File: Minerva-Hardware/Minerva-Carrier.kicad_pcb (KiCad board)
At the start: 4 copper layers, 83.5 x 90 mm, 59 parts, among them J1 HDMI_D_1.4, J11 USB_C_Receptacle_USB2.0, J14 JST_SHBM04B-SRSS-TB, J16 Conn_01x22_Female, J2 Conn_02x07_Odd_Even, J4 Bus_M.2_Socket_M, J5 Conn_01x22_Female, J6 THD-02-R, J8 THD-20-R, Q2 RQ6E080AJ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

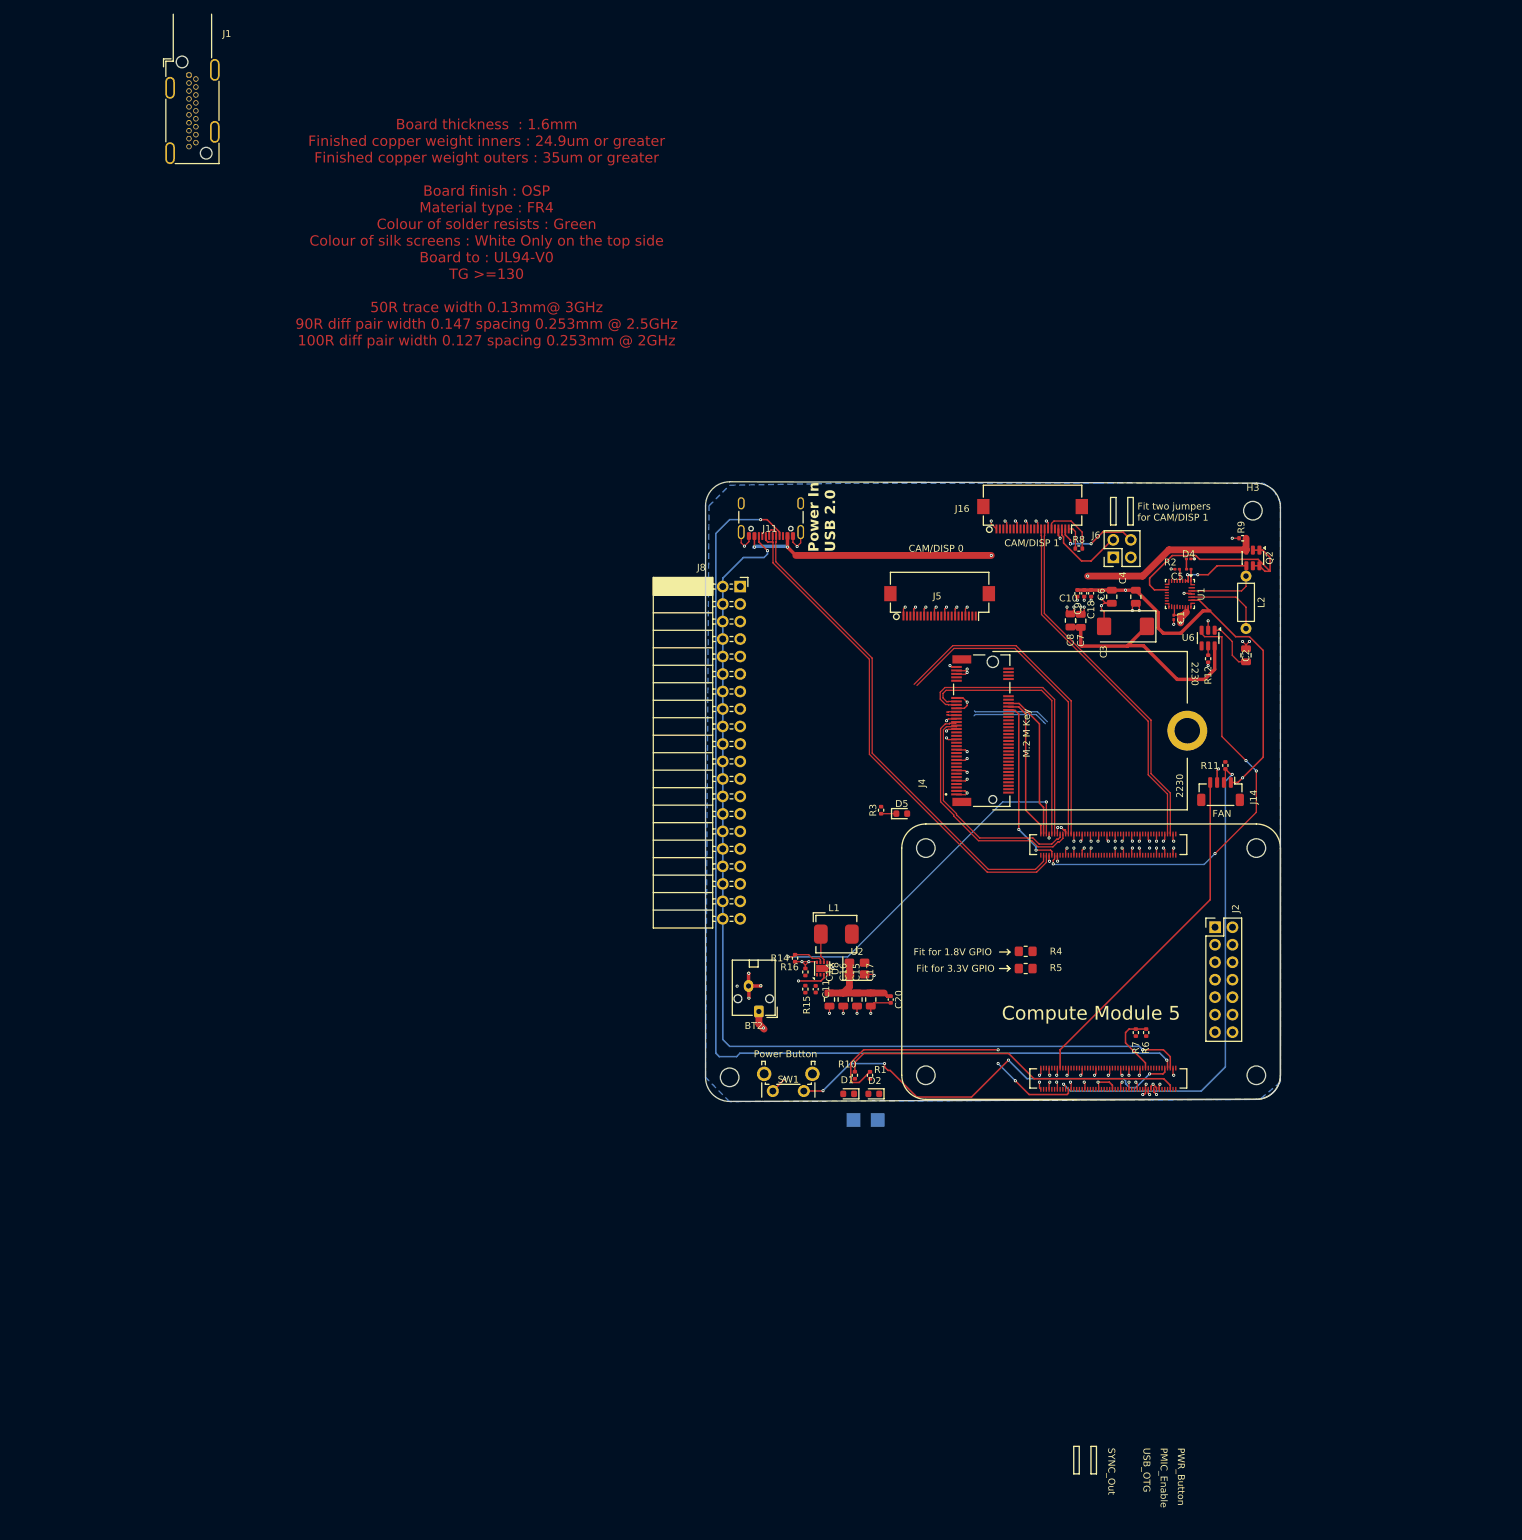
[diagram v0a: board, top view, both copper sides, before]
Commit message: Redid the BQ powerpath unit
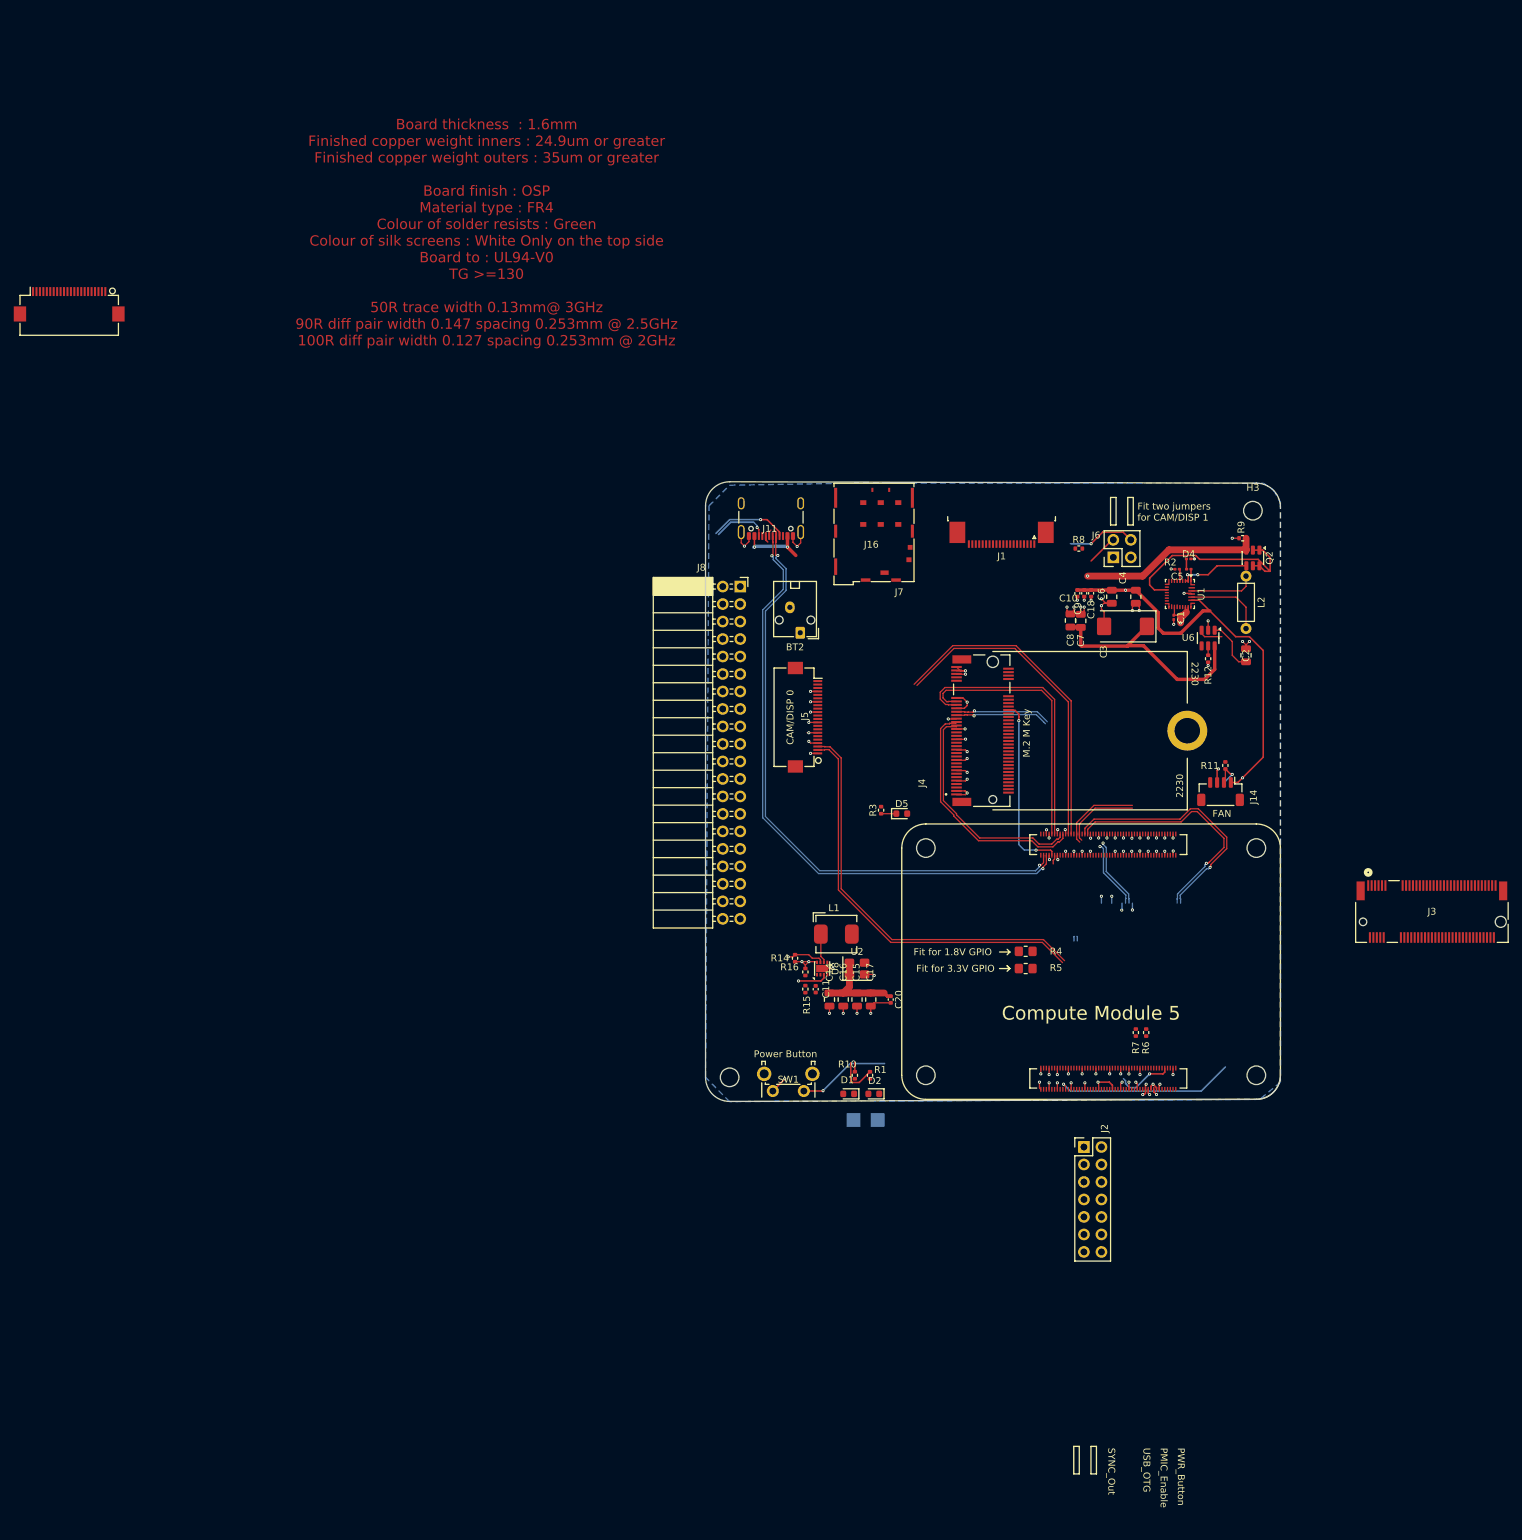
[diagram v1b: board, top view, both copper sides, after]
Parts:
- added J3: Bus_M.2_Socket_B, M.2B:CONN67_2199230_TEC, F.Cu at (193.8, 136.2)
- added J7: JAE_SIM_Card_SF72S006, Connector_JAE:JAE_SIM_Card_SF72S006, F.Cu at (104.4, 75.5)
- J1: footprint Connector_Video:HDMI_A_Kycon_KDMIX-SL1-NS-WS-B15_VerticalRightAngle -> Connector_FFC-FPC:TE_2-1734839-0_1x20-1MP_P0.5mm_Horizontal
- moved J16 143.3 mm to (-13.4, 44.2), turned to 0 degrees
- moved J1 135.6 mm to (122.0, 77.7), turned to 180 degrees
- moved BT2 55.3 mm to (92.8, 91.9)
- moved J2 37.2 mm to (134.0, 166.6)
- moved J5 25.6 mm to (93.5, 104.2), turned to -90 degrees
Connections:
- J1 pad 11: unconnected-(J1-D0--Pad11) -> /CM5_HighSpeed/HDMI_D0_N
- J1 pad 12: unconnected-(J1-CK+-Pad12) -> /CM5_HighSpeed/HDMI_CLK_P
- J1 pad 14: unconnected-(J1-CK--Pad14) -> /CM5_HighSpeed/HDMI_CLK_N
- J1 pad 15: unconnected-(J1-CEC-Pad15) -> /CM5_HighSpeed/HDMI_0_CEC
- J1 pad 16: unconnected-(J1-GND-Pad16) -> GND
- J1 pad 17: unconnected-(J1-SCL-Pad17) -> /CM5_HighSpeed/HDMI0_SCL
- J1 pad 18: unconnected-(J1-SDA-Pad18) -> /CM5_HighSpeed/HDMI0_SDA
- J1 pad 19: unconnected-(J1-+5V-Pad19) -> /CM5_HighSpeed/+5v
- J1 pad 3: unconnected-(J1-D2+-Pad3) -> /CM5_HighSpeed/HDMI_D2_P
- J1 pad 5: unconnected-(J1-D2--Pad5) -> /CM5_HighSpeed/HDMI_D2_N
- J1 pad 6: unconnected-(J1-D1+-Pad6) -> /CM5_HighSpeed/HDMI_D1_P
- J1 pad 8: unconnected-(J1-D1--Pad8) -> /CM5_HighSpeed/HDMI_D1_N
- J1 pad 9: unconnected-(J1-D0+-Pad9) -> /CM5_HighSpeed/HDMI_D0_P
- Module1 pad 151: unconnected-(Module1B-HDMI0_CEC-Pad151) -> /CM5_HighSpeed/HDMI_0_CEC
- Module1 pad 153: unconnected-(Module1B-HDMI0_HOTPLUG-Pad153) -> /CM5_HighSpeed/HDMI_0_HOTPLUG
- Module1 pad 170: unconnected-(Module1B-HDMI0_TX2_P-Pad170) -> /CM5_HighSpeed/HDMI_D2_P
- Module1 pad 172: unconnected-(Module1B-HDMI0_TX2_N-Pad172) -> /CM5_HighSpeed/HDMI_D2_N
- Module1 pad 176: unconnected-(Module1B-HDMI0_TX1_P-Pad176) -> /CM5_HighSpeed/HDMI_D1_P
- Module1 pad 178: unconnected-(Module1B-HDMI0_TX1_N-Pad178) -> /CM5_HighSpeed/HDMI_D1_N
- Module1 pad 182: unconnected-(Module1B-HDMI0_TX0_P-Pad182) -> /CM5_HighSpeed/HDMI_D0_P
- Module1 pad 184: unconnected-(Module1B-HDMI0_TX0_N-Pad184) -> /CM5_HighSpeed/HDMI_D0_N
- Module1 pad 188: unconnected-(Module1B-HDMI0_CLK_P-Pad188) -> /CM5_HighSpeed/HDMI_CLK_P
- Module1 pad 190: unconnected-(Module1B-HDMI0_CLK_N-Pad190) -> /CM5_HighSpeed/HDMI_CLK_N
- Module1 pad 199: unconnected-(Module1B-HDMI0_SDA-Pad199) -> /CM5_HighSpeed/HDMI0_SDA
- Module1 pad 200: unconnected-(Module1B-HDMI0_SCL-Pad200) -> /CM5_HighSpeed/HDMI0_SCL
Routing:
- net /CC1: track 154.4 -> 11.4 mm, vias 2 -> 1
- net /CC2: track 145.8 -> 8.11 mm, vias 3 -> 1
- net /CM5_HighSpeed/VBUS_EN: track 64.7 -> 4.48 mm, vias 4 -> 0
- net /CM5_HighSpeed/DPHY0_D0_P: track 0.00 -> 59.9 mm
- net /CM5_HighSpeed/DPHY0_D0_N: track 0.00 -> 59.5 mm
- net /CM5_HighSpeed/DPHY1_D3_P: track 51.9 -> 0.00 mm
- net /CM5_HighSpeed/DPHY1_D3_N: track 51.9 -> 0.00 mm
- net /CM5_HighSpeed/PCIE_PWR_EN: track 57.0 -> 6.13 mm
- net /CM5_GPIO/TACHO: track 50.5 -> 0.00 mm
- net /CM5_GPIO/nPWR_LED: track 50.2 -> 1.38 mm
- net /CM5_GPIO/PWM: track 71.8 -> 30.3 mm
- net /CM5_GPIO/PWR_BUT: track 62.1 -> 21.8 mm, vias 4 -> 2
- net /CM5_HighSpeed/USB3-0-D_P: track 0.00 -> 36.9 mm, vias 0 -> 1
- net /CM5_HighSpeed/USB3-0-D_N: track 0.00 -> 35.5 mm, vias 0 -> 1
- net Net-(Module1A-LED_nACT): track 43.1 -> 8.18 mm, vias 3 -> 0
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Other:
- board text removed: "CAM/DISP 1"
- board text removed: "Power In USB 2.0"

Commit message: working on pcb more
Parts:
- removed Q2: RQ6E080AJ, Package_TO_SOT_SMD:TSOT-23-6
- added C19: 0.1uF, Capacitor_SMD:C_01005_0402Metric, F.Cu at (252.8, 91.0)
- added C21: 10uF, Capacitor_SMD:C_01005_0402Metric, F.Cu at (252.8, 92.7)
- added C22: 10uF, Capacitor_SMD:C_01005_0402Metric, F.Cu at (252.8, 94.3)
- added C23: 10 uF, Capacitor_SMD:C_0201_0603Metric, F.Cu at (252.9, 99.3)
- added C24: 10uF, Capacitor_SMD:C_01005_0402Metric, F.Cu at (252.8, 96.0)
- added C25: 10uF, Capacitor_SMD:C_01005_0402Metric, F.Cu at (252.8, 97.6)
- added C26: 10uF, Capacitor_SMD:C_01005_0402Metric, F.Cu at (255.0, 91.0)
- added C27: 0.1uF, Capacitor_SMD:C_01005_0402Metric, F.Cu at (255.0, 92.7)
- added C28: 10uF, Capacitor_SMD:C_01005_0402Metric, F.Cu at (255.0, 94.3)
- added C29: 10uF, Capacitor_SMD:C_01005_0402Metric, F.Cu at (255.0, 96.0)
- added C30: 10uF, Capacitor_SMD:C_01005_0402Metric, F.Cu at (255.0, 97.6)
- added C31: 10uF, Capacitor_SMD:C_01005_0402Metric, F.Cu at (257.3, 91.0)
- added C32: 10uF, Capacitor_SMD:C_01005_0402Metric, F.Cu at (257.3, 92.7)
- added C33: 47nF, 25V X7R, Capacitor_SMD:C_01005_0402Metric, F.Cu at (257.3, 94.3)
- added C34: 47nF, 25V X7R, Capacitor_SMD:C_01005_0402Metric, F.Cu at (257.3, 96.0)
- C1: value C_Small_US -> 10 uF
- J3: moved to B.Cu
- L2: value 50 nH -> 1uH; footprint Inductor_THT:L_Axial_L5.3mm_D2.2mm_P7.62mm_Horizontal_Vishay_IM-1 -> CM5 IO Board-rev2:L_Bourns_SRP5030CC
- moved J3 62.8 mm to (131.0, 138.8), turned to 180 degrees
- moved J2 59.6 mm to (192.7, 176.6)
- moved J16 20.1 mm to (3.00, 55.8)
- moved J1 1.76 mm to (120.5, 78.6)
- moved J8 1.57 mm to (85.5, 85.7)
- moved J7 1.20 mm to (104.0, 76.6)
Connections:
- net /CHARGE_IND_SIG renamed +3.3V
- net Net-(U1-SW1) renamed /SW1
- net Net-(U1-SW2) renamed /SW2
- BT2 pad 1: Net-(BT2-+) -> /BATP
- C1 pad 1: Net-(BT2-+) -> /BATP
- C5 pad 1: Net-(U1-REGN) -> /REGN
- D1 pad 2: /+3.3v -> /CM5_GPIO/+3.3v
- D2 pad 2: /+3.3v -> /CM5_GPIO/+3.3v
- J1 pad 1: unconnected-(J1-HPD/HEAC--Pad1) -> /CM5_HighSpeed/HDMI_0_HOTPLUG
- J1 pad 10: unconnected-(J1-D0S-Pad10) -> GND
- J1 pad 13: unconnected-(J1-CKS-Pad13) -> GND
- J1 pad 2: unconnected-(J1-UTILITY/HEAC+-Pad2) -> /CM5_HighSpeed/HDMI_0_HOTPLUG
- J1 pad 4: unconnected-(J1-D2S-Pad4) -> GND
- J1 pad 7: unconnected-(J1-D1S-Pad7) -> GND
- J2 pad 10: /CM5_GPIO/USBOTG -> unconnected-(J2-Pin_10-Pad10)
- J8 pad 1: /+3.3v -> /CM5_GPIO/+3.3v
- J8 pad 17: /+3.3v -> /CM5_GPIO/+3.3v
- Module1 pad 157: /CM5_HighSpeed/USB3-1-RX_N -> GND
- Module1 pad 159: /CM5_HighSpeed/USB3-1-RX_P -> GND
- Module1 pad 163: /CM5_HighSpeed/USB3-1-D_P -> GND
- Module1 pad 165: /CM5_HighSpeed/USB3-1-D_N -> GND
- Module1 pad 169: /CM5_HighSpeed/USB3-1-TX_N -> GND
- Module1 pad 171: /CM5_HighSpeed/USB3-1-TX_P -> GND
- Module1 pad 84: /+3.3v -> /CM5_GPIO/+3.3v
- Module1 pad 86: /+3.3v -> /CM5_GPIO/+3.3v
- R11 pad 1: /+3.3v -> /CM5_GPIO/+3.3v
- R5 pad 1: /+3.3v -> /CM5_GPIO/+3.3v
- U1 pad 10: unconnected-(U1-ACDRV2-Pad10) -> GND
- U1 pad 11: Net-(U1-ACDRV1) -> GND
- U1 pad 12: unconnected-(U1-~{QON}-Pad12) -> /QON
- U1 pad 13: unconnected-(U1-~{CE}-Pad13) -> GND
- U1 pad 16: unconnected-(U1-TS-Pad16) -> Net-(U1-TS)
- U1 pad 17: unconnected-(U1-ILIM_HIZ-Pad17) -> /REGN
- U1 pad 18: Net-(BT2-+) -> Net-(U1-BATP)
- U1 pad 19: unconnected-(U1-BTST2-Pad19) -> /BTST2
- U1 pad 2: Net-(Q2-S) -> /VBUS
- U1 pad 20: unconnected-(U1-PROG-Pad20) -> Net-(U1-PROG)
- U1 pad 22: Net-(BT2-+) -> /BATP
- U1 pad 23: Net-(BT2-+) -> /BATP
- U1 pad 25: /+5v -> /SYS_OUT
- U1 pad 29: unconnected-(U1-PMID-Pad29) -> Net-(U1-PMID)
- U1 pad 3: Net-(Q2-S) -> /VBUS
- U1 pad 4: unconnected-(U1-BTST1-Pad4) -> /BTST1
- U1 pad 5: Net-(U1-REGN) -> /REGN
- U1 pad 8: unconnected-(U1-VAC2-Pad8) -> /VBUS
- U1 pad 9: unconnected-(U1-VAC1-Pad9) -> /VBUS
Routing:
- net (no net): track 0.00 -> 134.8 mm, vias 0 -> 1
- net Net-(BT2-+): track 93.0 -> 0.00 mm, vias 1 -> 0
- net Net-(U1-ACDRV1): track 31.4 -> 0.00 mm
- net Net-(Q2-S): track 10.4 -> 0.00 mm, vias 2 -> 0
- net Net-(U1-SW1): track 0.00 -> 9.67 mm
- net /SW1: track 9.67 -> 0.00 mm
- net Net-(U1-REGN): track 1.62 -> 0.00 mm
- net /REGN: track 0.00 -> 1.62 mm
- net /VBUS: vias 3 -> 5

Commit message: wip shit
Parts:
- moved C7 6.06 mm to (130.0, 85.2)
- moved C8 6.06 mm to (128.5, 85.2)
- turned J1 to 0 degrees
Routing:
- net /CM5_HighSpeed/HDMI_D2_P: track 0.00 -> 54.1 mm
- net /CM5_HighSpeed/HDMI_D2_N: track 0.00 -> 54.1 mm
- net /CM5_HighSpeed/HDMI_D1_P: track 0.00 -> 53.9 mm
- net /CM5_HighSpeed/HDMI_D1_N: track 0.00 -> 53.9 mm
- net /CM5_HighSpeed/HDMI_D0_N: track 0.00 -> 53.8 mm
- net /CM5_HighSpeed/HDMI_D0_P: track 0.00 -> 53.8 mm
- net /CM5_HighSpeed/HDMI_CLK_P: track 0.00 -> 53.7 mm
- net /CM5_HighSpeed/HDMI_CLK_N: track 0.00 -> 53.7 mm
- net /CM5_HighSpeed/DPHY0_D0_P: track 59.9 -> 33.5 mm
- net /CM5_HighSpeed/DPHY0_D0_N: track 59.5 -> 33.4 mm
- net GND: track 128.6 -> 144.0 mm, vias 102 -> 126
- net /CM5_HighSpeed/VBUS: track 33.7 -> 24.3 mm
- net /CM5_HighSpeed/USB3-0-TX_P: track 0.69 -> 8.64 mm
- net /CM5_HighSpeed/USB3-0-TX_N: track 0.69 -> 8.62 mm
- net /CM5_HighSpeed/USB3-0-RX_N: track 22.6 -> 15.1 mm
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
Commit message: Update Minerva-Carrier.kicad_pcb
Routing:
- net /CM5_HighSpeed/HDMI_0_HOTPLUG: track 0.00 -> 60.2 mm, vias 0 -> 2
- net /CM5_HighSpeed/PCIE_nWAKE: track 0.00 -> 22.0 mm
- net /CM5_HighSpeed/PCIE_nCLKREQ: track 0.00 -> 21.0 mm
- net /USB2_N: track 91.2 -> 89.7 mm
- net /USB2_P: track 91.4 -> 89.9 mm
- net /CM5_HighSpeed/PCIE_nRST: vias 3 -> 2
- net GND: vias 126 -> 132

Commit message: need to improve diff pair routing
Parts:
- moved C19 72.6 mm to (181.3, 103.9)
- moved C21 72.6 mm to (181.3, 105.5)
- moved C22 72.6 mm to (181.3, 107.2)
- moved C23 72.6 mm to (181.4, 112.2)
- moved C24 72.6 mm to (181.3, 108.8)
- moved C25 72.6 mm to (181.3, 110.5)
- moved C26 72.6 mm to (183.5, 103.9)
- moved C27 72.6 mm to (183.5, 105.5)
- moved C28 72.6 mm to (183.5, 107.2)
- moved C29 72.6 mm to (183.5, 108.8)
- moved C30 72.6 mm to (183.5, 110.5)
- moved C31 72.6 mm to (185.8, 103.9)
- moved C32 72.6 mm to (185.8, 105.5)
- moved C33 72.6 mm to (185.8, 107.2)
- moved C34 72.6 mm to (185.8, 108.8)
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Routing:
- net /CM5_HighSpeed/DPHY0_D3_N: track 0.00 -> 63.6 mm
- net /CM5_HighSpeed/DPHY0_D3_P: track 0.00 -> 62.9 mm
- net /CM5_HighSpeed/DPHY0_D2_P: track 0.00 -> 13.5 mm
- net /CM5_HighSpeed/DPHY0_D2_N: track 0.00 -> 13.1 mm
- net /CM5_HighSpeed/DPHY0_C_P: track 0.00 -> 12.1 mm
- net /CM5_HighSpeed/DPHY0_C_N: track 0.00 -> 11.8 mm
- net /CM5_HighSpeed/DPHY0_D1_P: track 0.00 -> 11.2 mm
- net /CM5_HighSpeed/DPHY0_D1_N: track 0.00 -> 10.8 mm
- net /CM5_HighSpeed/DPHY0_D0_P: track 33.5 -> 41.8 mm
- net /CM5_HighSpeed/DPHY0_D0_N: track 33.4 -> 41.0 mm
- net /CM5_HighSpeed/USB3-0-D_N: track 30.2 -> 34.2 mm
- net /CM5_HighSpeed/USB3-0-D_P: track 31.7 -> 35.3 mm
- net Net-(D5-K): track 2.20 -> 0.00 mm
- net /CM5_HighSpeed/USB3-0-TX_P: track 8.64 -> 10.8 mm, vias 0 -> 1
- net /CM5_HighSpeed/USB3-0-TX_N: track 8.62 -> 10.7 mm, vias 0 -> 1
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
